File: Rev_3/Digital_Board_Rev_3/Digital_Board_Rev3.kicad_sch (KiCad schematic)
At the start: 35 parts, among them J1 Conn_01x02_Male, J11 Conn_01x10_Female, J13 Conn_01x06_Female, J14 Conn_01x06_Female, J15 Conn_01x03_Male, J2 Conn_01x02_Male, J3 Conn_01x06_Male, J4 Conn_01x08_Female, SW5 SW_Push, U1 STM32F303R6Tx, Y1 8MHz

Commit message: Pivoting to Passive Jack Boards
Finalized layout for input/output Jack Boards, which are now completely passive and connected with board-to-board connectors. Schematics are not updated yet, just figuring out placement/dimensions.
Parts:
- removed C1: 4.7u, Capacitor_SMD:C_0805_2012Metric_Pad1.18x1.45mm_HandSolder, symbol Device:C
- removed C10: 1u, Capacitor_SMD:C_0805_2012Metric_Pad1.18x1.45mm_HandSolder, symbol Device:C
- removed C17, C20, C4, C5, C6, C7, C8: 100n, Capacitor_SMD:C_0805_2012Metric_Pad1.18x1.45mm_HandSolder, symbol Device:C
- removed C2, C3: 18p, Capacitor_SMD:C_0805_2012Metric_Pad1.18x1.45mm_HandSolder, symbol Device:C
- removed C9: 10n, Capacitor_SMD:C_0805_2012Metric_Pad1.18x1.45mm_HandSolder, symbol Device:C
- removed J1, J2: Conn_01x02_Male, Connector_PinHeader_2.54mm:PinHeader_1x02_P2.54mm_Vertical, symbol Digital Board Rev 2-rescue:Conn_01x02_Male-Connector
- removed J11: Conn_01x10_Female, Connector_PinSocket_2.54mm:PinSocket_1x10_P2.54mm_Vertical, symbol Digital Board Rev 2-rescue:Conn_01x10_Female-Connector
- removed J13, J14: Conn_01x06_Female, Connector_PinSocket_2.54mm:PinSocket_1x06_P2.54mm_Vertical, symbol Digital Board Rev 2-rescue:Conn_01x06_Female-Connector
- removed J15: Conn_01x03_Male, Connector_PinHeader_2.54mm:PinHeader_1x03_P2.54mm_Vertical, symbol Digital Board Rev 2-rescue:Conn_01x03_Male-Connector
- removed J3: Conn_01x06_Male, Connector_PinHeader_2.54mm:PinHeader_1x06_P2.54mm_Vertical, symbol Digital Board Rev 2-rescue:Conn_01x06_Male-Connector
- removed J4: Conn_01x08_Female, Connector_PinSocket_2.54mm:PinSocket_1x08_P2.54mm_Vertical, symbol Digital Board Rev 2-rescue:Conn_01x08_Female-Connector
- removed JP1: Jumper, Jumper:SolderJumper-2_P1.3mm_Bridged2Bar_Pad1.0x1.5mm, symbol Digital-Board-Rev-2-rescue:Jumper-Device
- removed NT1, NT2, NT3, NT4: NetTie_2, symbol Device:NetTie_2
- removed R1: 10k, Resistor_SMD:R_0805_2012Metric_Pad1.20x1.40mm_HandSolder, symbol Device:R
- removed R10, R11, R2, R3, R4, R5: 330, Resistor_SMD:R_0805_2012Metric_Pad1.20x1.40mm_HandSolder, symbol Device:R
- removed SW5: SW_Push, symbol Switch:SW_Push
- removed U1: STM32F303R6Tx, Package_QFP:LQFP-64_10x10mm_P0.5mm, symbol Digital Board Rev 2-rescue:STM32F303R6Tx-MCU_ST_STM32F3
- removed Y1: 8MHz, Crystal:Crystal_HC49-U_Vertical, symbol Device:Crystal
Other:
- sheet Harm/STD renamed Shape
- sheet SHAPE renamed PAN
- removed sheet Audio Jacks
- removed sheet ENV_MODE
- removed sheet LEDs
- removed sheet PAN_MODE
- removed sheet TAP EXP
- removed sheet VOLUME
- added sheet ENVELOPE (Envelope.kicad_sch)
- added sheet ENV_SW (sw_tactile.kicad_sch)
- added sheet Input Board Analog (InputBoard_Analog.kicad_sch)
- added sheet Input Board Digital (Input_Board_Digital.kicad_sch)
- added sheet Optos and LEDs (Optos_LEDs.kicad_sch)
- added sheet Output Board (OutputBoard.kicad_sch)
- sheet SUBDIV: file 10kPot.kicad_sch -> RotarySW_1P8T.kicad_sch
- sheet SUBDIV ports: added B0, B1, B2; removed WIPER
- note removed: "TAP_EXT on 5V tolerant pin"

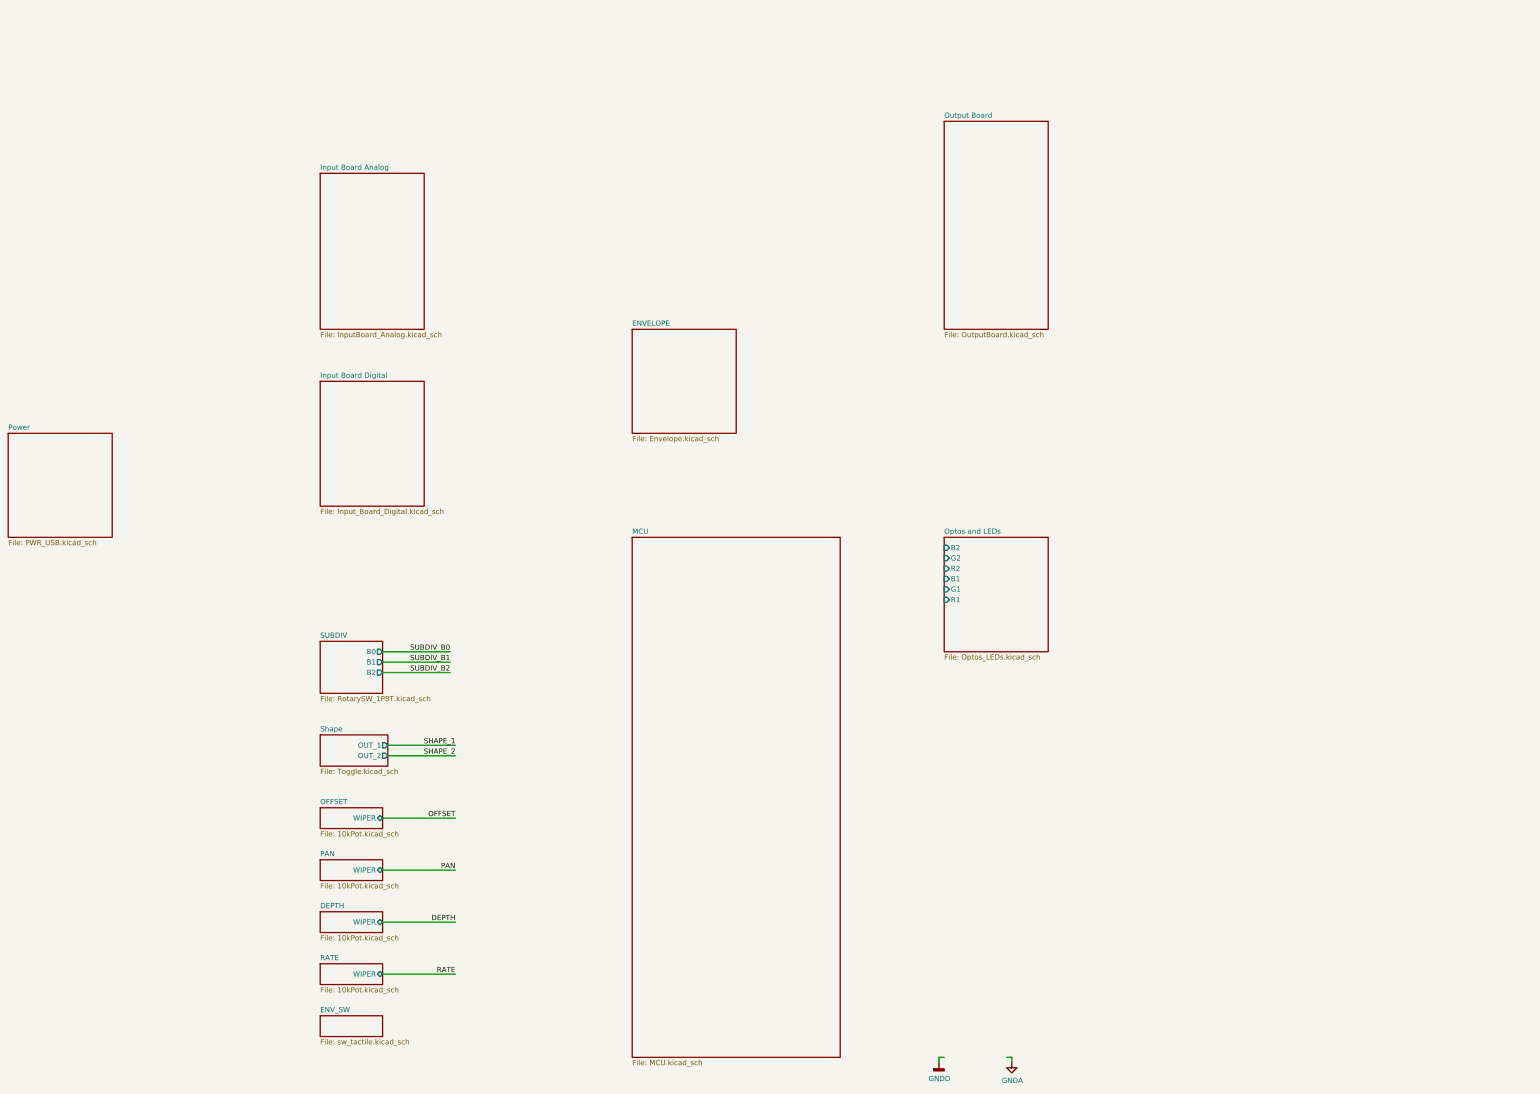
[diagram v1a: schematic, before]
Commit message: Added analog board back, switched to Jacks on Bottom
Added analog board mezzanine back to fit everything. Finalized decision on jack boards; jacks on bottom, wire to board connectors between jack boards and digital board. Tentative board outlines defined and scoped out component placement.
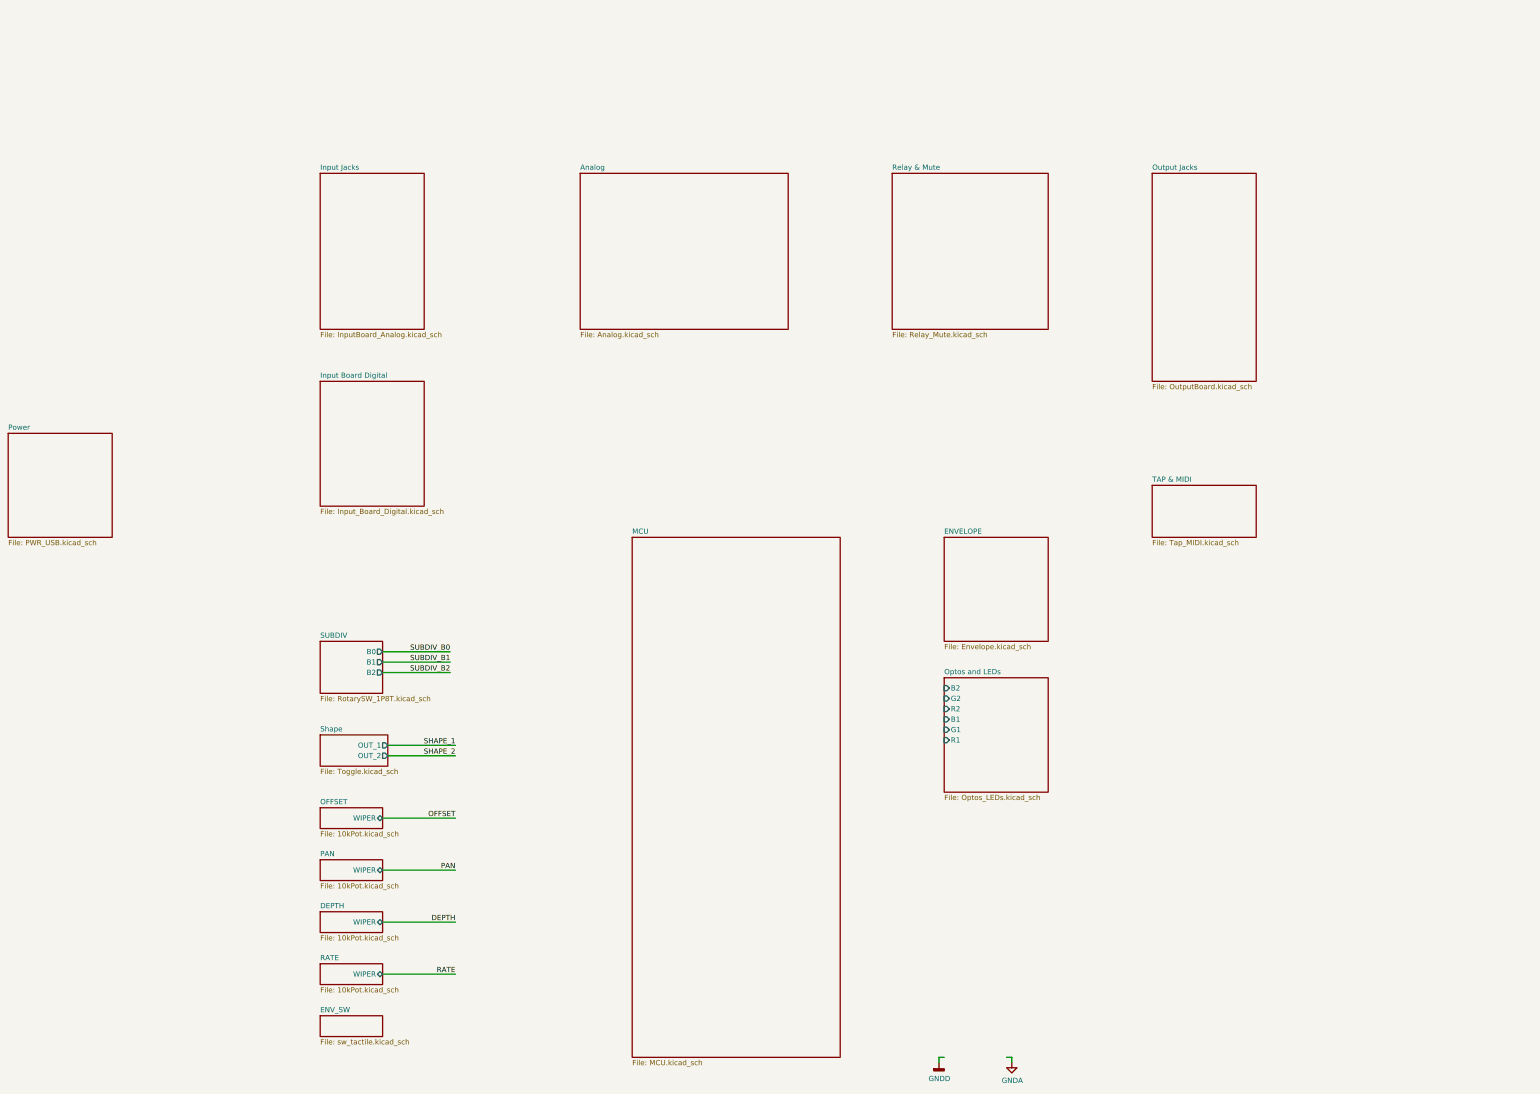
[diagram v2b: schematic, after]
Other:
- sheet Input Board Analog renamed Input Jacks
- sheet Output Board renamed Output Jacks
- added sheet Analog (Analog.kicad_sch)
- added sheet Relay & Mute (Relay_Mute.kicad_sch)
- added sheet TAP & MIDI (Tap_MIDI.kicad_sch)
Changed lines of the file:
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@@
 	)
 	(sheet
-		(at 254 25.4)
+		(at 304.8 38.1)
 		(size 25.4 50.8)
 		(exclude_from_sim no)
@@
 			(color 0 0 0 0.0000)
 		)
-		(property "Sheetname" "Output Board"
-			(at 254 24.6884 0)
+		(property "Sheetname" "Output Jacks"
+			(at 304.8 37.3884 0)
 			(effects
 				(font
@@
 		)
 		(property "Sheetfile" "OutputBoard.kicad_sch"
-			(at 254 76.7846 0)
+			(at 304.8 89.4846 0)
 			(effects
 				(font
@@
 	)
 	(sheet
-		(at 177.8 76.2)
+		(at 254 127)
 		(size 25.4 25.4)
 		(exclude_from_sim no)
@@
 		)
 		(property "Sheetname" "ENVELOPE"
-			(at 177.8 75.4884 0)
+			(at 254 126.2884 0)
 			(effects
 				(font
@@
 		)
 		(property "Sheetfile" "Envelope.kicad_sch"
-			(at 177.8 102.1846 0)
+			(at 254 152.9846 0)
+			(effects
+				(font
+					(size 1.27 1.27)
+				)
+				(justify left top)
+			)
+		)
+		(instances
+			(project "Digital_Board_Rev3"
+				(path "/961bce4d-0f15-4753-8332-e4f92c717c57"
+					(page "16")
+				)
+			)
+		)
+	)
+	(sheet
+		(at 165.1 38.1)
+		(size 50.8 38.1)
+		(exclude_from_sim no)
+		(in_bom yes)
+		(on_board yes)
+		(dnp no)
+		(fields_autoplaced yes)
+		(stroke
+			(width 0.1524)
+			(type solid)
+		)
+		(fill
+			(color 0 0 0 0.0000)
+		)
+		(property "Sheetname" "Analog"
+			(at 165.1 37.3884 0)
+			(effects
+				(font
+					(size 1.27 1.27)
+				)
+				(justify left bottom)
+			)
+		)
+		(property "Sheetfile" "Analog.kicad_sch"
+			(at 165.1 76.7846 0)
 			(effects
 				(font
@@
 	)
 	(sheet
+		(at 241.3 38.1)
+		(size 38.1 38.1)
+		(exclude_from_sim no)
+		(in_bom yes)
+		(on_board yes)
+		(dnp no)
+		(fields_autoplaced yes)
+		(stroke
+			(width 0.1524)
+			(type solid)
+		)
+		(fill
+			(color 0 0 0 0.0000)
+		)
+		(property "Sheetname" "Relay & Mute"
+			(at 241.3 37.3884 0)
+			(effects
+				(font
+					(size 1.27 1.27)
+				)
+				(justify left bottom)
+			)
+		)
+		(property "Sheetfile" "Relay_Mute.kicad_sch"
+			(at 241.3 76.7846 0)
+			(effects
+				(font
+					(size 1.27 1.27)
+				)
+				(justify left top)
+			)
+		)
+		(instances
+			(project "Digital_Board_Rev3"
+				(path "/961bce4d-0f15-4753-8332-e4f92c717c57"
+					(page "17")
+				)
+			)
+		)
+	)
+	(sheet
+		(at 304.8 114.3)
+		(size 25.4 12.7)
+		(exclude_from_sim no)
+		(in_bom yes)
+		(on_board yes)
+		(dnp no)
+		(fields_autoplaced yes)
+		(stroke
+			(width 0.1524)
+			(type solid)
+		)
+		(fill
+			(color 0 0 0 0.0000)
+		)
+		(property "Sheetname" "TAP & MIDI"
+			(at 304.8 113.5884 0)
+			(effects
+				(font
+					(size 1.27 1.27)
+				)
+				(justify left bottom)
+			)
+		)
+		(property "Sheetfile" "Tap_MIDI.kicad_sch"
+			(at 304.8 127.5846 0)
+			(effects
+				(font
+					(size 1.27 1.27)
+				)
+				(justify left top)
+			)
+		)
+		(instances
+			(project "Digital_Board_Rev3"
+				(path "/961bce4d-0f15-4753-8332-e4f92c717c57"
+					(page "18")
+				)
+			)
+		)
+	)
+	(sheet
 		(at 101.6 243.84)
 		(size 15.24 5.08)
@@
 			(color 0 0 0 0.0000)
 		)
-		(property "Sheetname" "Input Board Analog"
+		(property "Sheetname" "Input Jacks"
 			(at 101.6 37.3884 0)
 			(effects
@@
 	)
 	(sheet
-		(at 254 127)
+		(at 254 161.29)
 		(size 25.4 27.94)
 		(exclude_from_sim no)
@@
 		)
 		(property "Sheetname" "Optos and LEDs"
-			(at 254 126.2884 0)
+			(at 254 160.5784 0)
 			(effects
 				(font
@@
 		)
 		(property "Sheetfile" "Optos_LEDs.kicad_sch"
-			(at 254 155.5246 0)
+			(at 254 189.8146 0)
 			(effects
 				(font
@@
 		)
 		(pin "R1" input
-			(at 254 142.24 180)
+			(at 254 176.53 180)
 			(effects
 				(font
@@
 		)
 		(pin "G1" input
-			(at 254 139.7 180)
+			(at 254 173.99 180)
 			(effects
 				(font
@@
 		)
 		(pin "B1" input
-			(at 254 137.16 180)
+			(at 254 171.45 180)
 			(effects
 				(font
@@
 		)
 		(pin "R2" input
-			(at 254 134.62 180)
+			(at 254 168.91 180)
 			(effects
 				(font
@@
 		)
 		(pin "G2" input
-			(at 254 132.08 180)
+			(at 254 166.37 180)
 			(effects
 				(font
@@
 		)
 		(pin "B2" input
-			(at 254 129.54 180)
-			(effects
-				(font
+			(at 254 163.83 180)
+			(effects
+				(font

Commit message: Backing up before windows crash debug
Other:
- sheet Analog renamed Analog Board Connectors
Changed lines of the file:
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@@
 			(color 0 0 0 0.0000)
 		)
-		(property "Sheetname" "Analog"
+		(property "Sheetname" "Analog Board Connectors"
 			(at 165.1 37.3884 0)
 			(effects
